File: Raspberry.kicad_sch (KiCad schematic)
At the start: 15 parts, among them J19 Raspberry_Pi_2_3, J25 Conn_02x06_Top_Bottom, U3 PCA9634PW,118, U4 MCP2515-xSO, U5 MCP2562-E-SN, Y1 16MHz

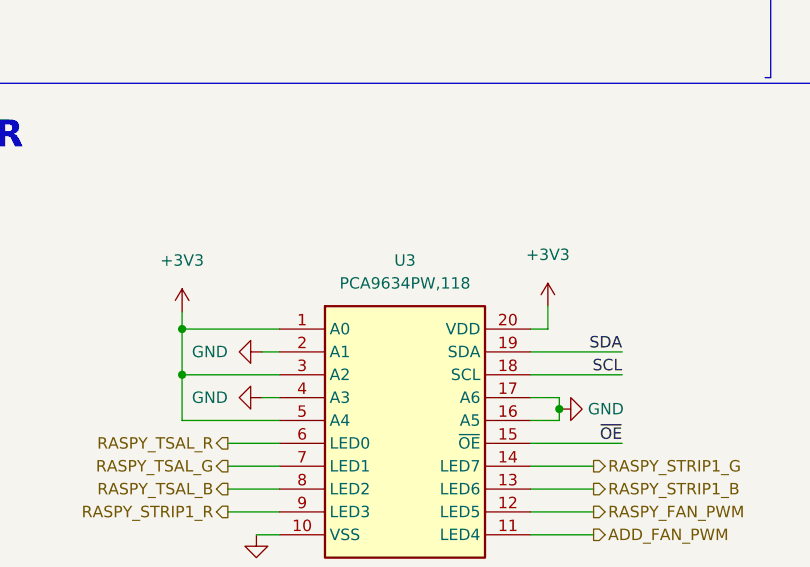
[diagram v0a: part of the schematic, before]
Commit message: Changed mosfet, fixed all the datasheets, added 3D models
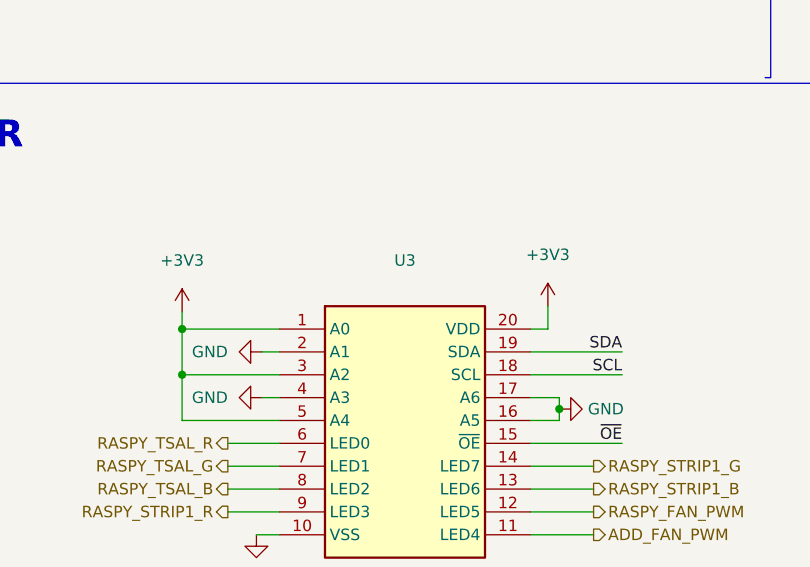
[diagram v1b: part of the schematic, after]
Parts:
- J25: footprint Connector_Molex:Molex_Micro-Fit_3.0_43045-1000_2x05_P3.00mm_Horizontal -> Connector_Molex:Molex_Micro-Fit_3.0_43045-1012_2x05_P3.00mm_Vertical
- U3: Datasheet_1 http://www.nxp.com/docs/en/data-sheet/PCA9634.pdf -> (none); Footprint_1 SOP65P640X110-20N -> (none); Reference_1 IC -> (none); Value_1 PCA9634PW,118 -> (none)
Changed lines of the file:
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@@
       (effects (font (size 1.27 1.27) italic) hide)
     )
-    (property "Datasheet" "http://ww1.microchip.com/downloads/en/DeviceDoc/25167A.pdf" (id 3) (at 236.22 64.135 0)
+    (property "Datasheet" "datasheets/25167A.pdf" (id 3) (at 236.22 64.135 0)
       (effects (font (size 1.27 1.27)) hide)
     )
@@
       (effects (font (size 1.27 1.27)) hide)
     )
-    (property "Datasheet" "https://www.raspberrypi.org/documentation/hardware/raspberrypi/schematics/rpi_SCH_3bplus_1p0_reduced.pdf" (id 3) (at 74.295 69.215 0)
+    (property "Datasheet" "datasheets/raspberry-pi-3-b-plus-reduced-schematics.pdf" (id 3) (at 74.295 69.215 0)
       (effects (font (size 1.27 1.27)) hide)
     )
@@
     (property "Reference" "J25" (id 0) (at 32.385 102.235 0))
     (property "Value" "Conn_02x06_Top_Bottom" (id 1) (at 32.385 104.775 0))
-    (property "Footprint" "Connector_Molex:Molex_Micro-Fit_3.0_43045-1000_2x05_P3.00mm_Horizontal" (id 2) (at 31.75 114.3 0)
+    (property "Footprint" "Connector_Molex:Molex_Micro-Fit_3.0_43045-1012_2x05_P3.00mm_Vertical" (id 2) (at 31.75 114.3 0)
       (effects (font (size 1.27 1.27)) hide)
     )
@@
       (effects (font (size 1.27 1.27) italic) hide)
     )
-    (property "Datasheet" "http://ww1.microchip.com/downloads/en/DeviceDoc/21801e.pdf" (id 3) (at 180.34 92.075 0)
+    (property "Datasheet" "datasheets/MCP2515.pdf" (id 3) (at 180.34 92.075 0)
       (effects (font (size 1.27 1.27)) hide)
     )
@@
       (effects (font (size 1.27 1.27)) hide)
     )
-    (property "Datasheet" "" (id 3) (at 72.39 152.4 0)
-      (effects (font (size 1.27 1.27)) hide)
-    )
-    (property "Reference_1" "IC" (id 4) (at 86.36 144.78 0)
-      (effects (font (size 1.27 1.27)) hide)
-    )
-    (property "Value_1" "PCA9634PW,118" (id 5) (at 86.36 147.32 0))
-    (property "Footprint_1" "SOP65P640X110-20N" (id 6) (at 96.52 247.32 0)
-      (effects (font (size 1.27 1.27)) (justify left top) hide)
-    )
-    (property "Datasheet_1" "http://www.nxp.com/docs/en/data-sheet/PCA9634.pdf" (id 7) (at 96.52 347.32 0)
-      (effects (font (size 1.27 1.27)) (justify left top) hide)
+    (property "Datasheet" "datasheets/PCA9634.pdf" (id 3) (at 72.39 152.4 0)
+      (effects (font (size 1.27 1.27)) hide)
     )
     (property "Height" "1.1" (id 8) (at 96.52 547.32 0)

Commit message: Major changes after the schematic review. Refer to Github for all the changes
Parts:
- added C? (x4): 100nF, Resistor_SMD:R_0805_2012Metric, symbol Device:C
- added D2: 1N4148W, Diode_SMD:D_SOD-323_HandSoldering, symbol Device:D_Small
- added J20: RASPI_FAN, Connector_Molex:Molex_Micro-Fit_3.0_43650-0215_1x02_P3.00mm_Vertical, symbol Connector_Generic:Conn_01x02
- added JP2: 3V3_RASPI, symbol Jumper:SolderJumper_2_Open
- added Q2: 2N7002NXAK, Package_TO_SOT_SMD:SOT-23, symbol Device:Q_NMOS_GSD
- added R6: 22R, Resistor_SMD:R_0603_1608Metric, symbol Device:R
- added R7: 330k, Resistor_SMD:R_0603_1608Metric, symbol Device:R
- J18: renamed from J25; value Conn_02x06_Top_Bottom -> SPARE_RASPI
- R3: renamed from R1; value 10k -> 4k7; footprint Resistor_SMD:R_0805_2012Metric -> Resistor_SMD:R_0603_1608Metric
- R4: renamed from R2; value 10k -> 4k7; footprint Resistor_SMD:R_0805_2012Metric -> Resistor_SMD:R_0603_1608Metric
- R5: renamed from R3; value 10k -> 4k7; footprint Resistor_SMD:R_0805_2012Metric -> Resistor_SMD:R_0603_1608Metric
- R8: renamed from R120; value R -> 120R; footprint Resistor_SMD:R_0805_2012Metric -> Resistor_SMD:R_0603_1608Metric
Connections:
- net +3V3: now also C?.1, C?.1, C?.1, JP2.2 (B); no longer J19.1 (3V3), J19.17 (3V3)
- net +5V: now also C?.1, D2.1 (K), J20.1 (Pin_1)
- net GND: now also C?.2, C?.2, C?.2, C?.2, Q2.2 (S), R7.2
- net NC_RASP_8: no longer J19.12 (GPIO18/PWM0)
- net RASPY_FAN_PWM: now also R6.2
- new net: Q2.1 (G), R6.1, R7.1
- new net: D2.2 (A), J20.2 (Pin_2), Q2.3 (D)
- new net: J19.1 (3V3), J19.17 (3V3), JP2.1 (A)
- new net ADD_RGB_STRIP: J19.12 (GPIO18/PWM0)
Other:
- note added: "RASPI FAN"
- moved on the sheet: C1, C2, C3, C4, C5, J18, J19, R3, R4, R5, R8, U3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

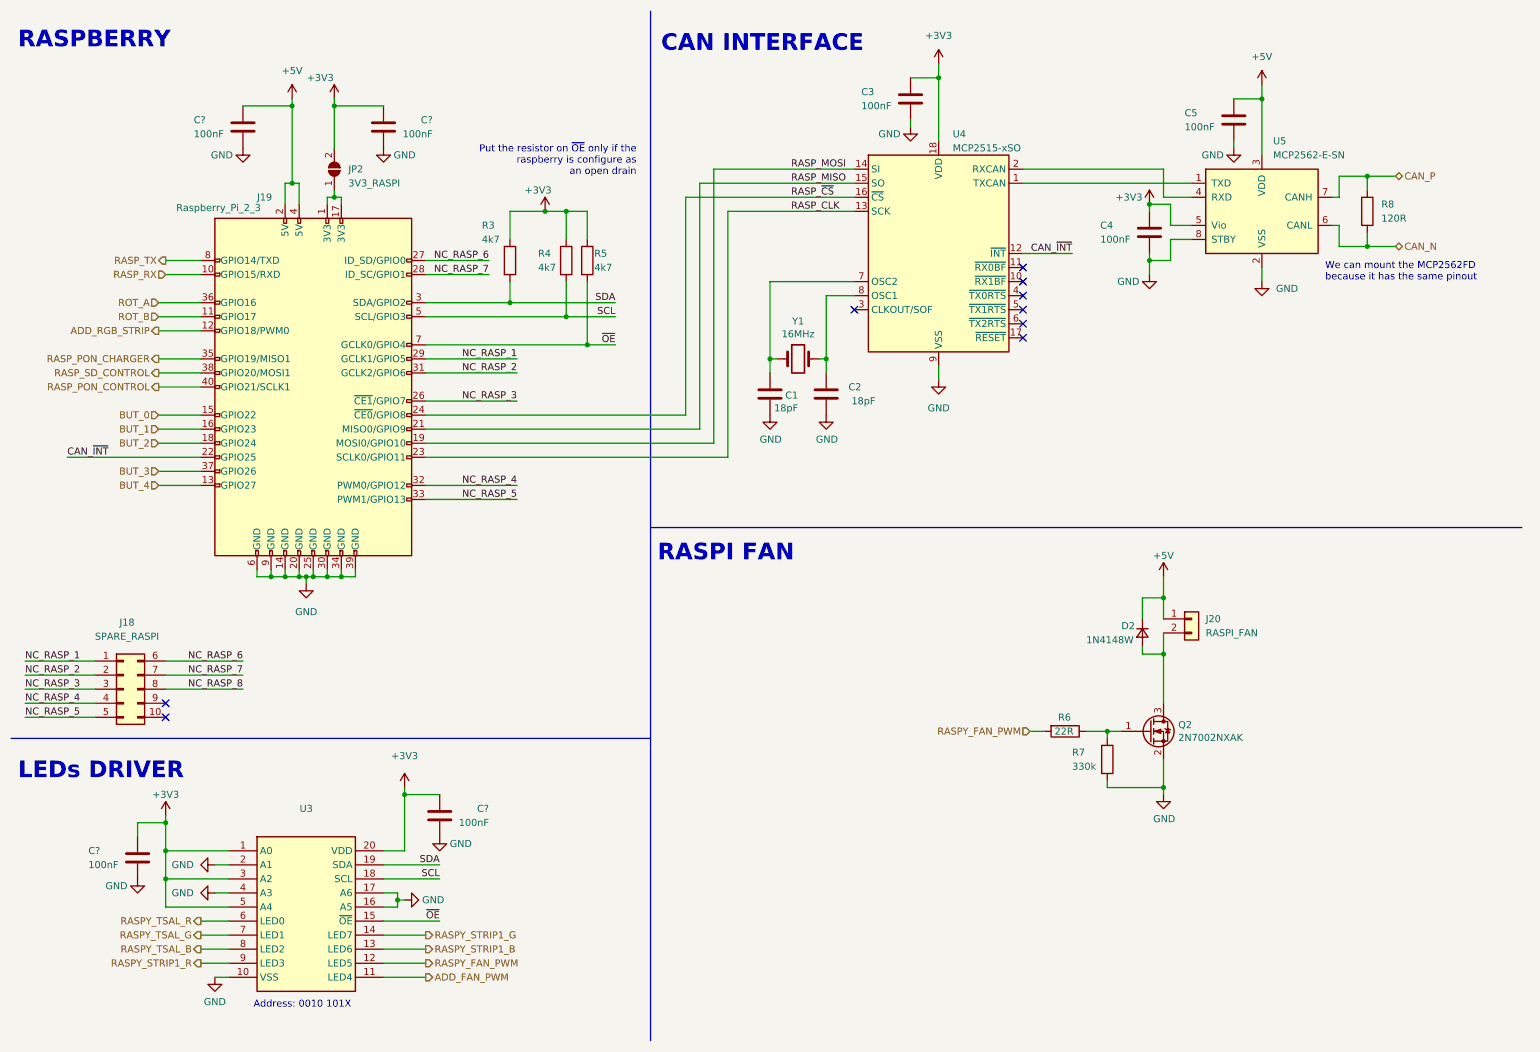
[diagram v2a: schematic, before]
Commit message: modified schematic and started design pcb
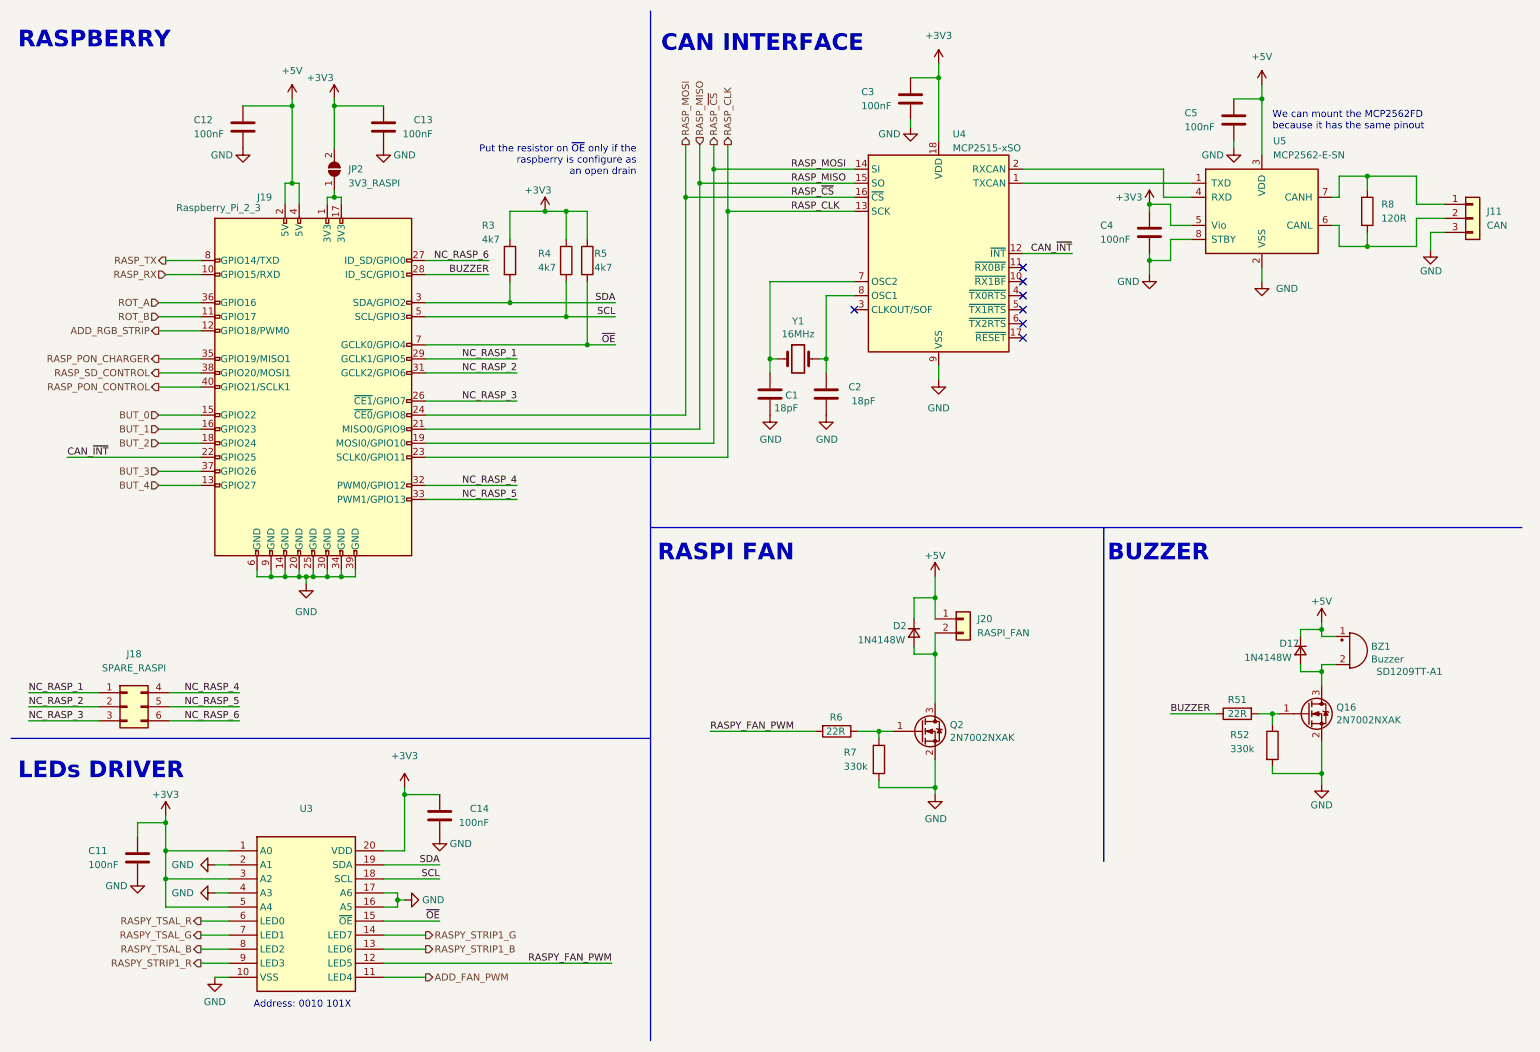
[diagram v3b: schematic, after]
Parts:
- added BZ1: Buzzer, Buzzer_Beeper:Buzzer_TDK_PS1240P02BT_D12.2mm_H6.5mm, symbol Device:Buzzer
- added D17: 1N4148W, Diode_SMD:D_SOD-323_HandSoldering, symbol Device:D_Small
- added J11: CAN, Connector_Molex:Molex_Micro-Fit_3.0_43650-0300_1x03_P3.00mm_Horizontal, symbol Connector_Generic:Conn_01x03
- added Q16: 2N7002NXAK, Package_TO_SOT_SMD:SOT-23, symbol Device:Q_NMOS_GSD
- added R51: 22R, Resistor_SMD:R_0603_1608Metric, symbol Device:R
- added R52: 330k, Resistor_SMD:R_0603_1608Metric, symbol Device:R
- J18: footprint Connector_Molex:Molex_Micro-Fit_3.0_43045-1012_2x05_P3.00mm_Vertical -> Connector_Molex:Molex_Micro-Fit_3.0_43045-0612_2x03_P3.00mm_Vertical; symbol Connector_Generic:Conn_02x05_Top_Bottom -> Connector_Generic:Conn_02x03_Top_Bottom
- JP2: footprint (none) -> Jumper:SolderJumper-2_P1.3mm_Open_RoundedPad1.0x1.5mm
- gave numbers to parts that had none: 4
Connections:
- net RASP_~{CS} is gone; now on net RASP_MOSI: J19.24 (~{CE0}/GPIO8), U4.16 (~{CS})
- net +5V: now also BZ1.1 (-), D17.1 (K)
- net GND: now also J11.3 (Pin_3), Q16.2 (S), R52.2
- net CAN_N: no longer names the net of R8.2, U5.6 (CANL)
- net CAN_N: now also J11.2 (Pin_2)
- net CAN_P: no longer names the net of R8.1, U5.7 (CANH)
- net CAN_P: now also J11.1 (Pin_1)
- net NC_RASP_7 renamed BUZZER
- net BUZZER: now also R51.1; no longer J18.7 (Pin_7)
- removed net NC_RASP_8: J18.8 (Pin_8)
- new net: BZ1.2 (+), D17.2 (A), Q16.3 (D)
- new net: Q16.1 (G), R51.2, R52.1
- no-connect marks 9 -> 7
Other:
- note added: "BUZZER"
- moved on the sheet: D2, J20, Q2, R6, R7

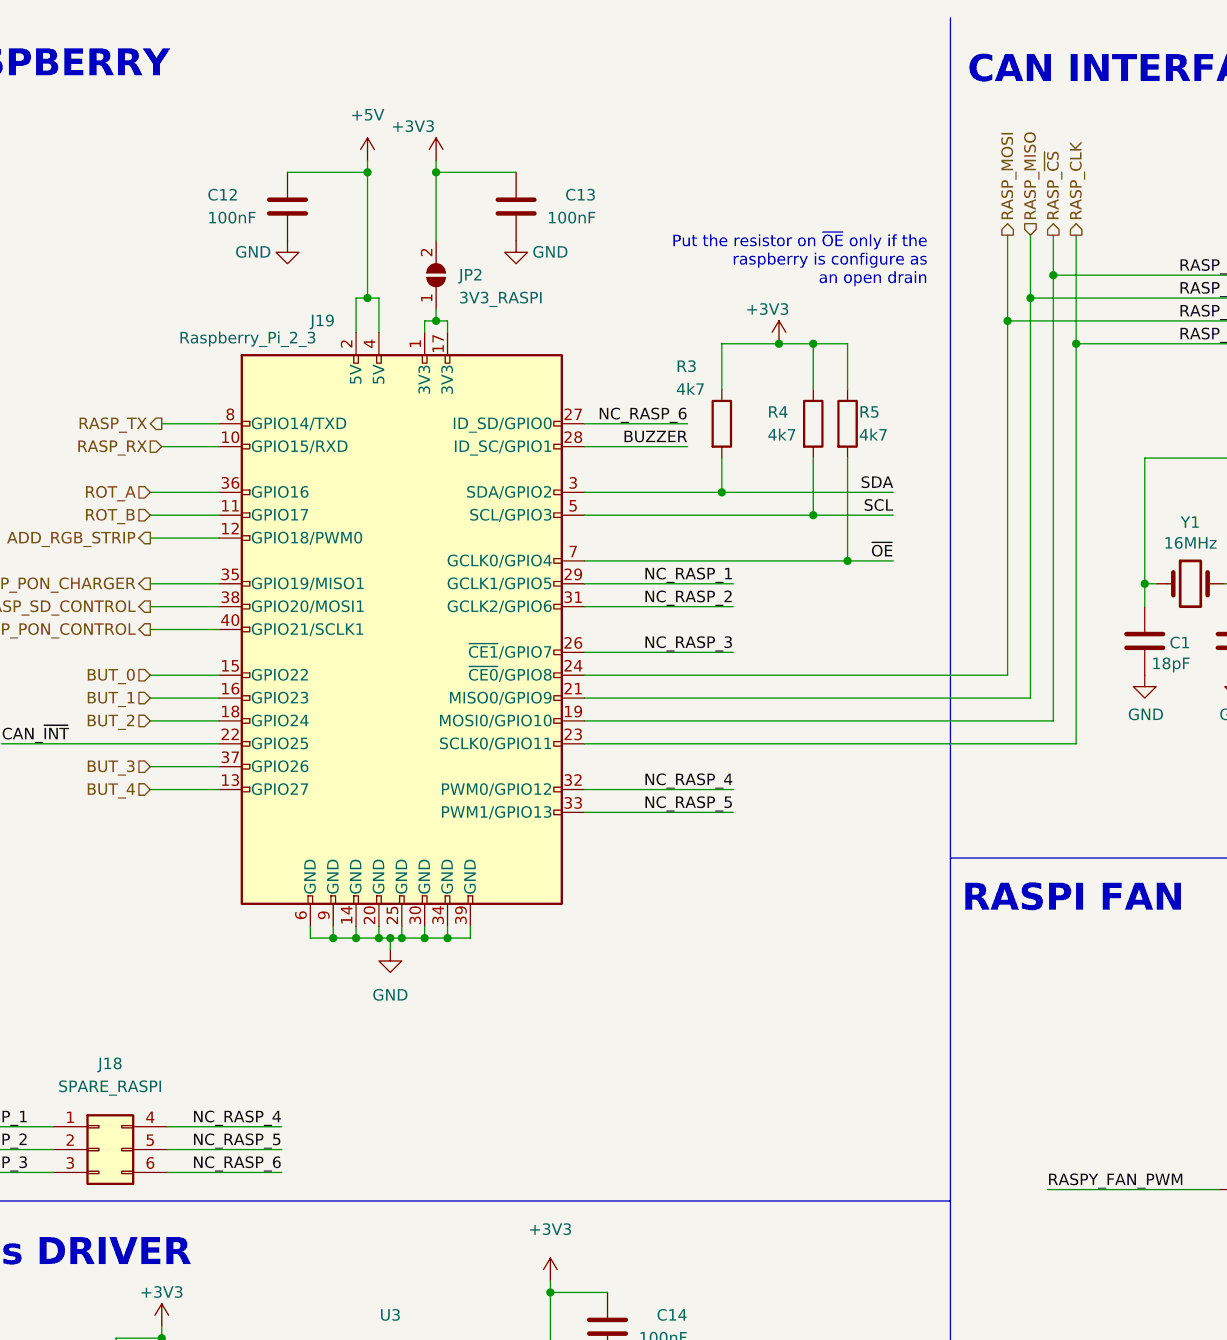
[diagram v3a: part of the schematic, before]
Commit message: Fixed frequency of LPF, added reverse polarity protection
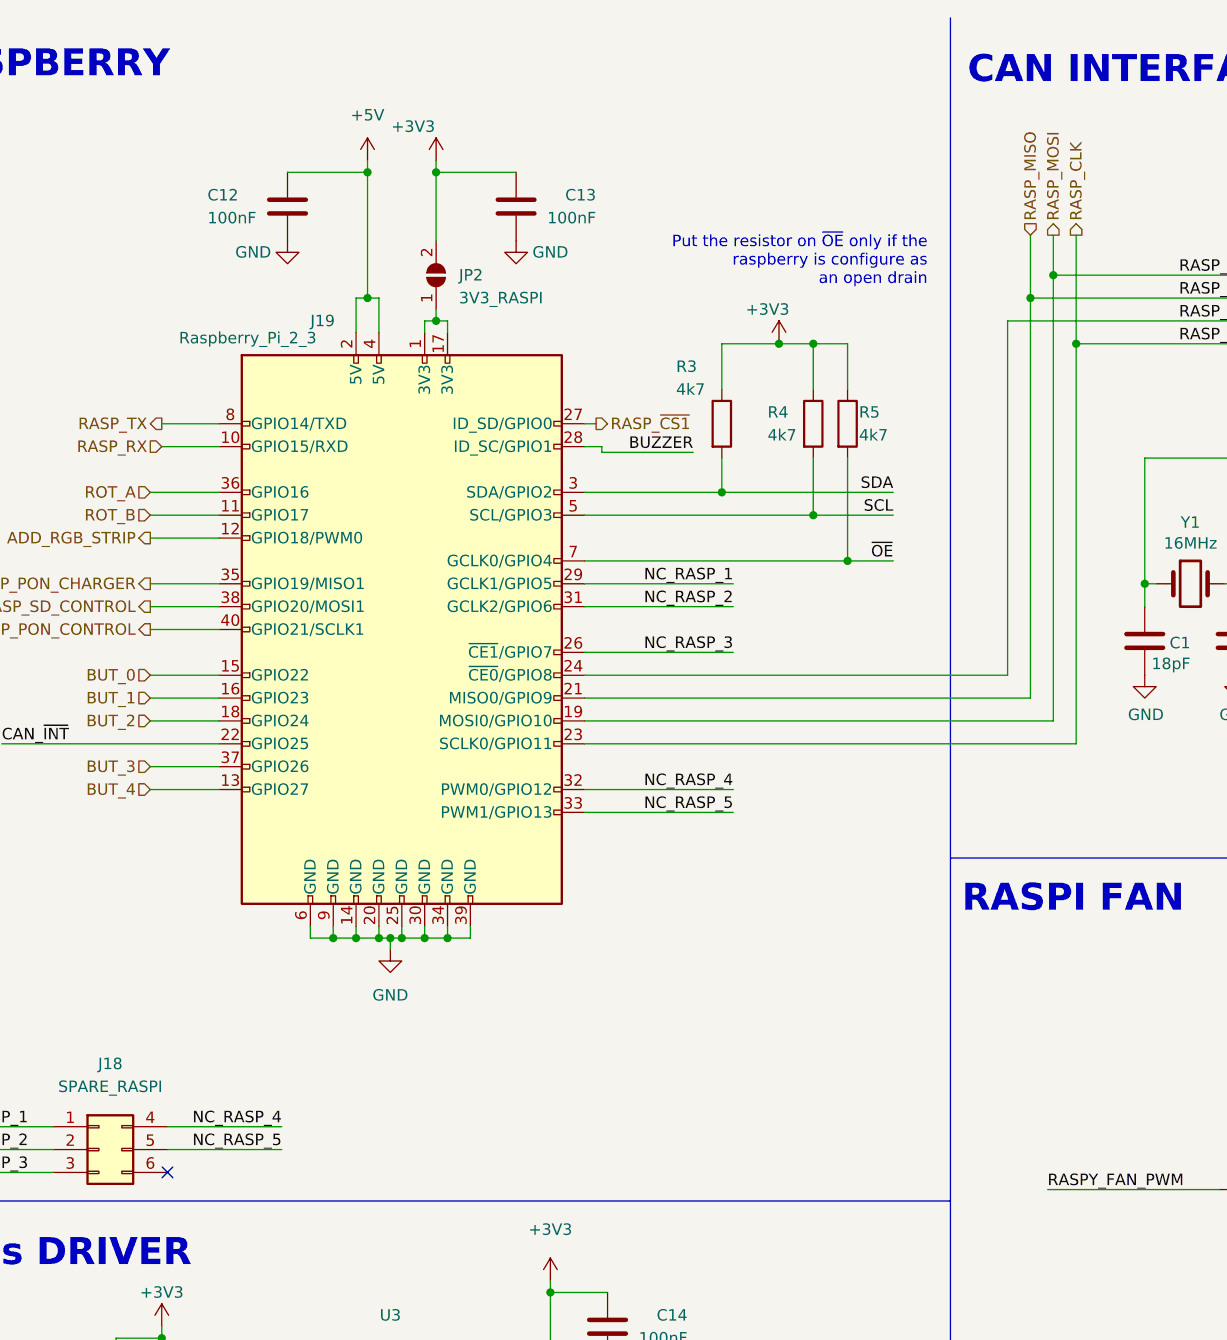
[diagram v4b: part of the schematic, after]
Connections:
- net RASP_MOSI: no longer J19.24 (~{CE0}/GPIO8), U4.16 (~{CS})
- net NC_RASP_6: no longer names the net of J18.6 (Pin_6)
- net NC_RASP_6: no longer J19.27 (ID_SD/GPIO0)
- new net RASP_~{CS1}: J19.27 (ID_SD/GPIO0)
- new net RASP_~{CS}: J19.24 (~{CE0}/GPIO8), U4.16 (~{CS})
- no-connect marks 7 -> 8
